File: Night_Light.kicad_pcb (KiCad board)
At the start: 2 copper layers, 25.4 x 25.4 mm, 6 parts, among them J1 3V0, Q1 2N3904

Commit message: Remove ground plane. Fixes #6
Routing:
- net GND: track 0.00 -> 22.0 mm
- removed copper zone on F.Cu, net GND
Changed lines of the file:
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@@
   (segment (start 136.7 97.79) (end 131.572 97.79) (width 0.5) (layer "B.Cu") (net 3))
   (segment (start 131.572 97.79) (end 129.286 95.504) (width 0.5) (layer "B.Cu") (net 3))
+  (segment (start 145.91 97.79) (end 149.606 94.094) (width 0.5) (layer "B.Cu") (net 4))
+  (segment (start 142.7 97.79) (end 145.91 97.79) (width 0.5) (layer "B.Cu") (net 4))
+  (segment (start 149.606 90.17) (end 149.606 80.518) (width 0.5) (layer "B.Cu") (net 4))
+  (segment (start 149.606 94.094) (end 149.606 90.17) (width 0.5) (layer "B.Cu") (net 4))
   (segment (start 139.446 92.964) (end 141.732 92.964) (width 0.5) (layer "B.Cu") (net 5))
   (segment (start 147.066 80.518) (end 147.066 84.328) (width 0.5) (layer "B.Cu") (net 5))
@@
   (segment (start 147.066 84.328) (end 144.526 86.868) (width 0.5) (layer "B.Cu") (net 5))
   (segment (start 144.526 86.868) (end 144.526 90.17) (width 0.5) (layer "B.Cu") (net 5))
-  (zone (net 4) (net_name "GND") (layer "F.Cu") (hatch edge 0.508)
-    (connect_pads (clearance 0.508))
-    (min_thickness 0.254) (filled_areas_thickness no)
-    (fill yes (thermal_gap 0.508) (thermal_bridge_width 0.508))
-    (polygon
-      (pts
-        (xy 154.94 104.14)
-        (xy 124.46 104.14)
-        (xy 124.46 73.66)
-        (xy 154.94 73.66)
-      )
-    )
-  )
   (group "" (id f62a1b55-27ae-43dd-a9ba-5872dc4d0301)
     (members

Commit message: Update PCB for new KiCad 7 libraries
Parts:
- R1: value 100K -> 10K
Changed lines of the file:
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@@
     (property "Sheetfile" "Night_Light.kicad_sch")
     (property "Sheetname" "")
+    (property "ki_description" "Light emitting diode")
+    (property "ki_keywords" "LED diode")
     (attr through_hole)
     (fp_text reference "D1" (at 5.593 0) (layer "F.SilkS")
@@
     (fp_circle (center 1.27 0) (end 3.77 0)
       (stroke (width 0.1) (type solid)) (fill none) (layer "F.Fab"))
-    (pad "1" thru_hole rect (at 0 0 180) (size 1.8 2) (drill 0.9) (layers "*.Cu" "*.Mask")
+    (pad "1" thru_hole rect (at 0 0 180) (size 1.8 1.8) (drill 0.9) (layers "*.Cu" "*.Mask")
       (net 1 "/Collecter") (pinfunction "K") (pintype "passive"))
-    (pad "2" thru_hole oval (at 2.54 0 180) (size 1.8 2.2) (drill 0.9) (layers "*.Cu" "*.Mask")
+    (pad "2" thru_hole circle (at 2.54 0 180) (size 1.8 1.8) (drill 0.9) (layers "*.Cu" "*.Mask")
       (net 2 "/LED +") (pinfunction "A") (pintype "passive"))
     (model "${KICAD6_3DMODEL_DIR}/LED_THT.3dshapes/LED_D5.0mm_Clear.wrl"
@@
     (property "Sheetfile" "Night_Light.kicad_sch")
     (property "Sheetname" "")
+    (property "ki_description" "Resistor")
+    (property "ki_keywords" "R res resistor")
     (attr through_hole)
     (fp_text reference "R3" (at 5.08 -2.37) (layer "F.SilkS")
@@
     (fp_line (start 10.16 0) (end 8.23 0)
       (stroke (width 0.1) (type solid)) (layer "F.Fab"))
-    (pad "1" thru_hole oval (at 0 0) (size 1.6 2) (drill 0.8) (layers "*.Cu" "*.Mask")
+    (pad "1" thru_hole circle (at 0 0) (size 1.6 1.6) (drill 0.8) (layers "*.Cu" "*.Mask")
       (net 3 "+3V0") (pintype "passive"))
-    (pad "2" thru_hole oval (at 10.16 0) (size 1.6 2) (drill 0.8) (layers "*.Cu" "*.Mask")
+    (pad "2" thru_hole oval (at 10.16 0) (size 1.6 1.6) (drill 0.8) (layers "*.Cu" "*.Mask")
       (net 2 "/LED +") (pintype "passive"))
     (model "${KICAD6_3DMODEL_DIR}/Resistor_THT.3dshapes/R_Axial_DIN0207_L6.3mm_D2.5mm_P10.16mm_Horizontal.wrl"
@@
     (property "Sheetfile" "Night_Light.kicad_sch")
     (property "Sheetname" "")
+    (property "ki_description" "NPN transistor, emitter/base/collector")
+    (property "ki_keywords" "transistor NPN")
     (attr through_hole)
     (fp_text reference "Q1" (at 2.54 -3.56 180) (layer "F.SilkS")
@@
     (fp_arc (start 2.54 -2.48) (mid 4.831221 -0.949055) (end 4.293625 1.753625)
       (stroke (width 0.1) (type solid)) (layer "F.Fab"))
-    (pad "1" thru_hole rect (at 0 0 180) (size 1.5 1.7) (drill 0.8) (layers "*.Cu" "*.Mask")
+    (pad "1" thru_hole rect (at 0 0 180) (size 1.5 1.5) (drill 0.8) (layers "*.Cu" "*.Mask")
       (net 4 "GND") (pinfunction "E") (pintype "passive"))
-    (pad "2" thru_hole oval (at 2.54 0 180) (size 1.5 1.9) (drill 0.8) (layers "*.Cu" "*.Mask")
+    (pad "2" thru_hole circle (at 2.54 0 180) (size 1.5 1.5) (drill 0.8) (layers "*.Cu" "*.Mask")
       (net 5 "/Base") (pinfunction "B") (pintype "passive"))
-    (pad "3" thru_hole oval (at 5.08 0 180) (size 1.5 1.9) (drill 0.8) (layers "*.Cu" "*.Mask")
+    (pad "3" thru_hole circle (at 5.08 0 180) (size 1.5 1.5) (drill 0.8) (layers "*.Cu" "*.Mask")
       (net 1 "/Collecter") (pinfunction "C") (pintype "passive"))
     (model "${KICAD6_3DMODEL_DIR}/Package_TO_SOT_THT.3dshapes/TO-92_Inline_Wide.wrl"
@@
     (property "Sheetfile" "Night_Light.kicad_sch")
     (property "Sheetname" "")
+    (property "ki_description" "Generic connector, single row, 01x02, script generated")
+    (property "ki_keywords" "connector")
     (attr exclude_from_pos_files)
     (fp_text reference "J1" (at -3.35 0) (layer "F.SilkS")
@@
     (fp_circle (center 6 0) (end 7.5 0)
       (stroke (width 0.1) (type solid)) (fill none) (layer "F.Fab"))
-    (pad "1" thru_hole roundrect (at 0 0) (size 3.1 3.5) (drill 2.1) (layers "*.Cu" "*.Mask") (roundrect_rratio 0.080645)
+    (pad "1" thru_hole roundrect (at 0 0) (size 3.1 3.1) (drill 2.1) (layers "*.Cu" "*.Mask") (roundrect_rratio 0.080645)
       (net 3 "+3V0") (pinfunction "Pin_1") (pintype "passive"))
-    (pad "2" thru_hole oval (at 6 0) (size 3.1 3.5) (drill 2.1) (layers "*.Cu" "*.Mask")
+    (pad "2" thru_hole circle (at 6 0) (size 3.1 3.1) (drill 2.1) (layers "*.Cu" "*.Mask")
       (net 4 "GND") (pinfunction "Pin_2") (pintype "passive"))
     (model "${KICAD6_3DMODEL_DIR}/Connector_Wire.3dshapes/SolderWire-1.5sqmm_1x02_P6mm_D1.7mm_OD3mm.wrl"
@@
     (property "Sheetfile" "Night_Light.kicad_sch")
     (property "Sheetname" "")
+    (property "ki_description" "Resistor")
+    (property "ki_keywords" "R res resistor")
     (attr through_hole)
     (fp_text reference "R1" (at 5.08 -2.37) (layer "F.SilkS")
         (effects (font (size 1 1) (thickness 0.1524)))
     )
-    (fp_text value "100K" (at 5.08 2.37) (layer "F.Fab")
+    (fp_text value "10K" (at 5.08 2.37) (layer "F.Fab")
         (effects (font (size 1 1) (thickness 0.15)))
     )
@@
     (fp_line (start 10.16 0) (end 8.23 0)
       (stroke (width 0.1) (type solid)) (layer "F.Fab"))
-    (pad "1" thru_hole oval (at 0 0) (size 1.6 2) (drill 0.8) (layers "*.Cu" "*.Mask")
+    (pad "1" thru_hole circle (at 0 0) (size 1.6 1.6) (drill 0.8) (layers "*.Cu" "*.Mask")
       (net 3 "+3V0") (pintype "passive"))
-    (pad "2" thru_hole oval (at 10.16 0) (size 1.6 2) (drill 0.8) (layers "*.Cu" "*.Mask")
+    (pad "2" thru_hole oval (at 10.16 0) (size 1.6 1.6) (drill 0.8) (layers "*.Cu" "*.Mask")
       (net 5 "/Base") (pintype "passive"))
     (model "${KICAD6_3DMODEL_DIR}/Resistor_THT.3dshapes/R_Axial_DIN0207_L6.3mm_D2.5mm_P10.16mm_Horizontal.wrl"
@@
     (property "Sheetfile" "Night_Light.kicad_sch")
     (property "Sheetname" "")
+    (property "ki_description" "Photoresistor")
+    (property "ki_keywords" "resistor variable light sensitive opto LDR")
     (attr through_hole)
     (fp_text reference "R2" (at 2.54 4.064) (layer "F.SilkS")
@@
     (fp_arc (start 4.84 -3) (mid 6.320211 -0.001572) (end 4.842494 2.998087)
       (stroke (width 0.1) (type solid)) (layer "F.Fab"))
-    (pad "1" thru_hole oval (at 0 0) (size 1.6 2) (drill 0.8) (layers "*.Cu" "*.Mask")
+    (pad "1" thru_hole circle (at 0 0) (size 1.6 1.6) (drill 0.8) (layers "*.Cu" "*.Mask")
       (net 5 "/Base") (pintype "passive"))
-    (pad "2" thru_hole oval (at 5.08 0) (size 1.6 2) (drill 0.8) (layers "*.Cu" "*.Mask")
+    (pad "2" thru_hole circle (at 5.08 0) (size 1.6 1.6) (drill 0.8) (layers "*.Cu" "*.Mask")
       (net 4 "GND") (pintype "passive"))
     (model "${KICAD6_3DMODEL_DIR}/OptoDevice.3dshapes/R_LDR_7x6mm_P5.1mm_Vertical.wrl"

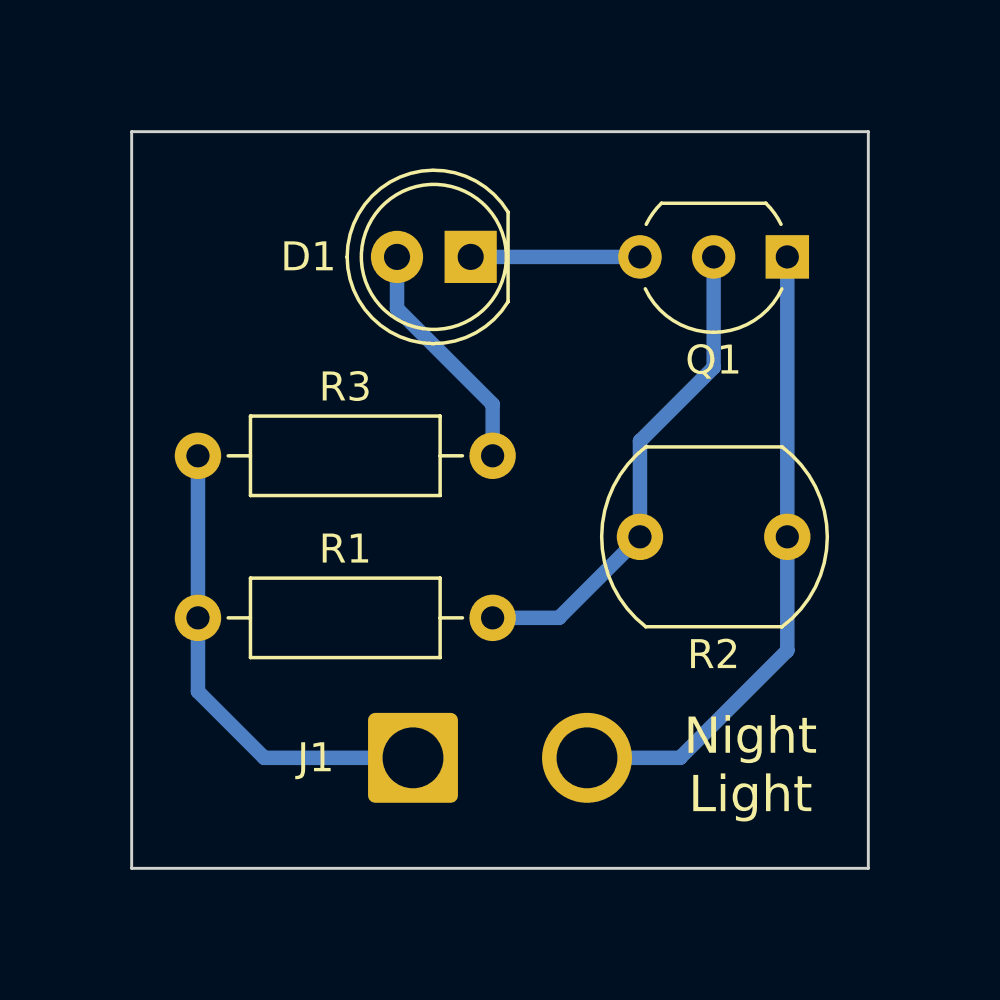
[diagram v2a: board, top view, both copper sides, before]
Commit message: Changed all track widths to 1mm. Fixes issue #5.
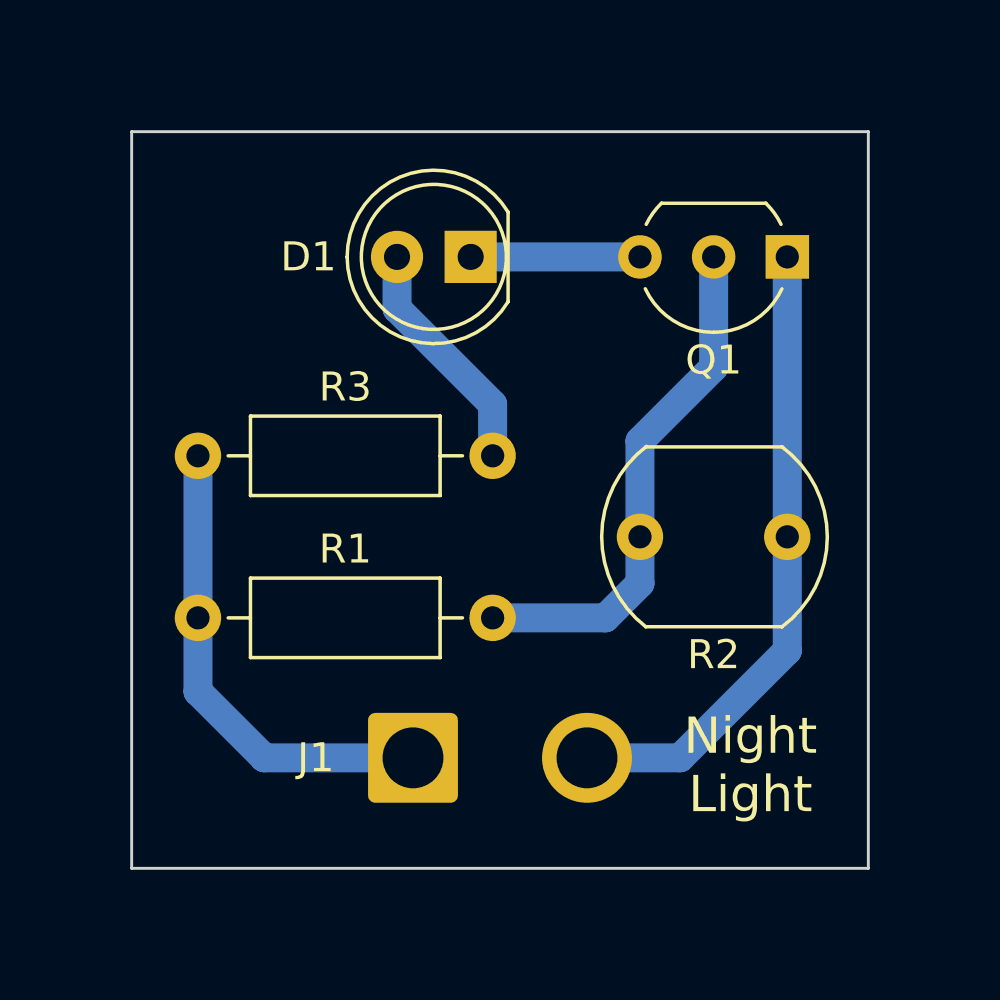
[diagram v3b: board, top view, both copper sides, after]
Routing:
- net /Base: track 16.9 -> 17.9 mm
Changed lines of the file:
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@@
     (effects (font (size 1.25 1.25) (thickness 0.2)))
   )
-  (segment (start 138.689 80.518) (end 144.526 80.518) (width 0.5) (layer "B.Cu") (net 1))
-  (segment (start 136.149 82.301) (end 139.446 85.598) (width 0.5) (layer "B.Cu") (net 2))
-  (segment (start 139.446 85.598) (end 139.446 87.376) (width 0.5) (layer "B.Cu") (net 2))
-  (segment (start 136.149 80.518) (end 136.149 82.301) (width 0.5) (layer "B.Cu") (net 2))
-  (segment (start 129.286 92.964) (end 129.286 87.376) (width 0.5) (layer "B.Cu") (net 3))
-  (segment (start 129.286 95.504) (end 129.286 92.964) (width 0.5) (layer "B.Cu") (net 3))
-  (segment (start 136.7 97.79) (end 131.572 97.79) (width 0.5) (layer "B.Cu") (net 3))
-  (segment (start 131.572 97.79) (end 129.286 95.504) (width 0.5) (layer "B.Cu") (net 3))
-  (segment (start 145.91 97.79) (end 149.606 94.094) (width 0.5) (layer "B.Cu") (net 4))
-  (segment (start 142.7 97.79) (end 145.91 97.79) (width 0.5) (layer "B.Cu") (net 4))
-  (segment (start 149.606 90.17) (end 149.606 80.518) (width 0.5) (layer "B.Cu") (net 4))
-  (segment (start 149.606 94.094) (end 149.606 90.17) (width 0.5) (layer "B.Cu") (net 4))
-  (segment (start 139.446 92.964) (end 141.732 92.964) (width 0.5) (layer "B.Cu") (net 5))
-  (segment (start 147.066 80.518) (end 147.066 84.328) (width 0.5) (layer "B.Cu") (net 5))
-  (segment (start 141.732 92.964) (end 144.526 90.17) (width 0.5) (layer "B.Cu") (net 5))
-  (segment (start 147.066 84.328) (end 144.526 86.868) (width 0.5) (layer "B.Cu") (net 5))
-  (segment (start 144.526 86.868) (end 144.526 90.17) (width 0.5) (layer "B.Cu") (net 5))
+  (segment (start 138.689 80.518) (end 144.526 80.518) (width 1) (layer "B.Cu") (net 1))
+  (segment (start 136.149 82.301) (end 139.446 85.598) (width 1) (layer "B.Cu") (net 2))
+  (segment (start 139.446 85.598) (end 139.446 87.376) (width 1) (layer "B.Cu") (net 2))
+  (segment (start 136.149 80.518) (end 136.149 82.301) (width 1) (layer "B.Cu") (net 2))
+  (segment (start 129.286 92.964) (end 129.286 87.376) (width 1) (layer "B.Cu") (net 3))
+  (segment (start 129.286 95.504) (end 129.286 92.964) (width 1) (layer "B.Cu") (net 3))
+  (segment (start 136.7 97.79) (end 131.572 97.79) (width 1) (layer "B.Cu") (net 3))
+  (segment (start 131.572 97.79) (end 129.286 95.504) (width 1) (layer "B.Cu") (net 3))
+  (segment (start 145.91 97.79) (end 149.606 94.094) (width 1) (layer "B.Cu") (net 4))
+  (segment (start 142.7 97.79) (end 145.91 97.79) (width 1) (layer "B.Cu") (net 4))
+  (segment (start 149.606 90.17) (end 149.606 80.518) (width 1) (layer "B.Cu") (net 4))
+  (segment (start 149.606 94.094) (end 149.606 90.17) (width 1) (layer "B.Cu") (net 4))
+  (segment (start 144.526 91.774) (end 144.526 90.17) (width 1) (layer "B.Cu") (net 5))
+  (segment (start 147.066 80.518) (end 147.066 84.328) (width 1) (layer "B.Cu") (net 5))
+  (segment (start 139.446 92.964) (end 143.336 92.964) (width 1) (layer "B.Cu") (net 5))
+  (segment (start 143.336 92.964) (end 144.526 91.774) (width 1) (layer "B.Cu") (net 5))
+  (segment (start 147.066 84.328) (end 144.526 86.868) (width 1) (layer "B.Cu") (net 5))
+  (segment (start 144.526 86.868) (end 144.526 90.17) (width 1) (layer "B.Cu") (net 5))
   (group "" (id f62a1b55-27ae-43dd-a9ba-5872dc4d0301)
     (members
